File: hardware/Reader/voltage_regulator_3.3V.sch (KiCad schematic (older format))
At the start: 8 parts

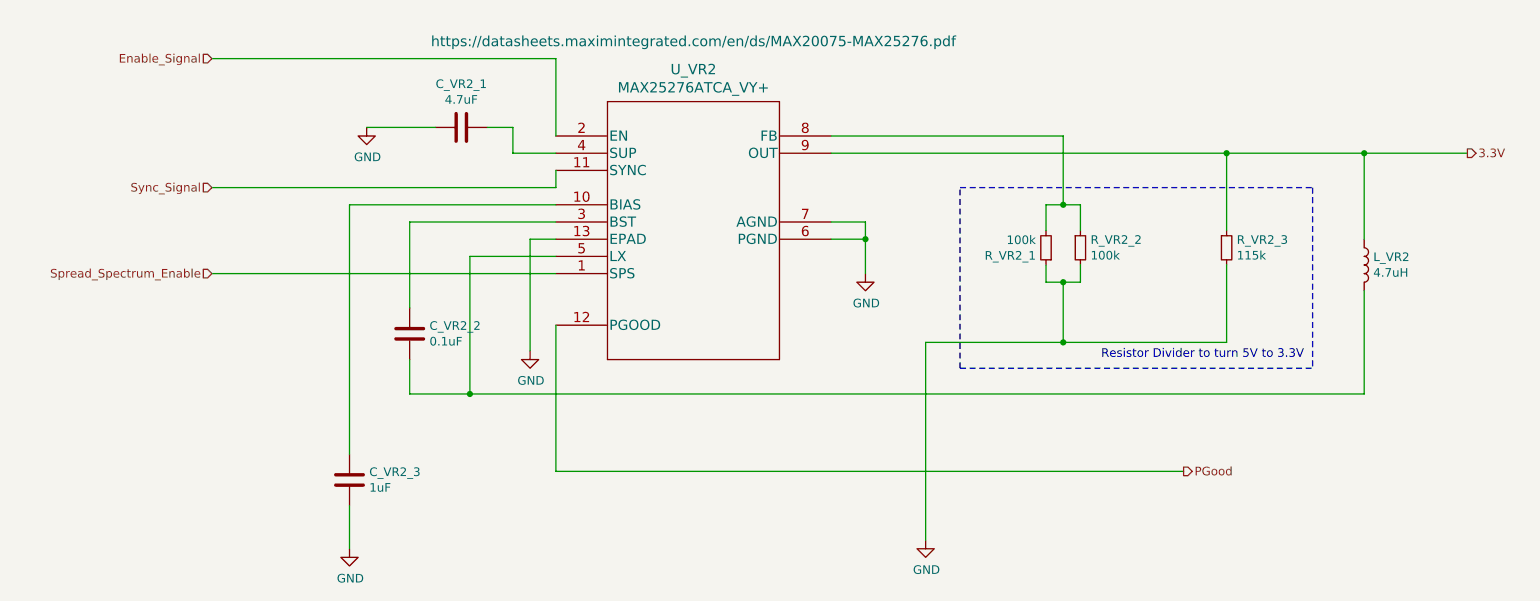
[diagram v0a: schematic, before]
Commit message: Fixed numerous bugs in design for Reader Schematic and PCB
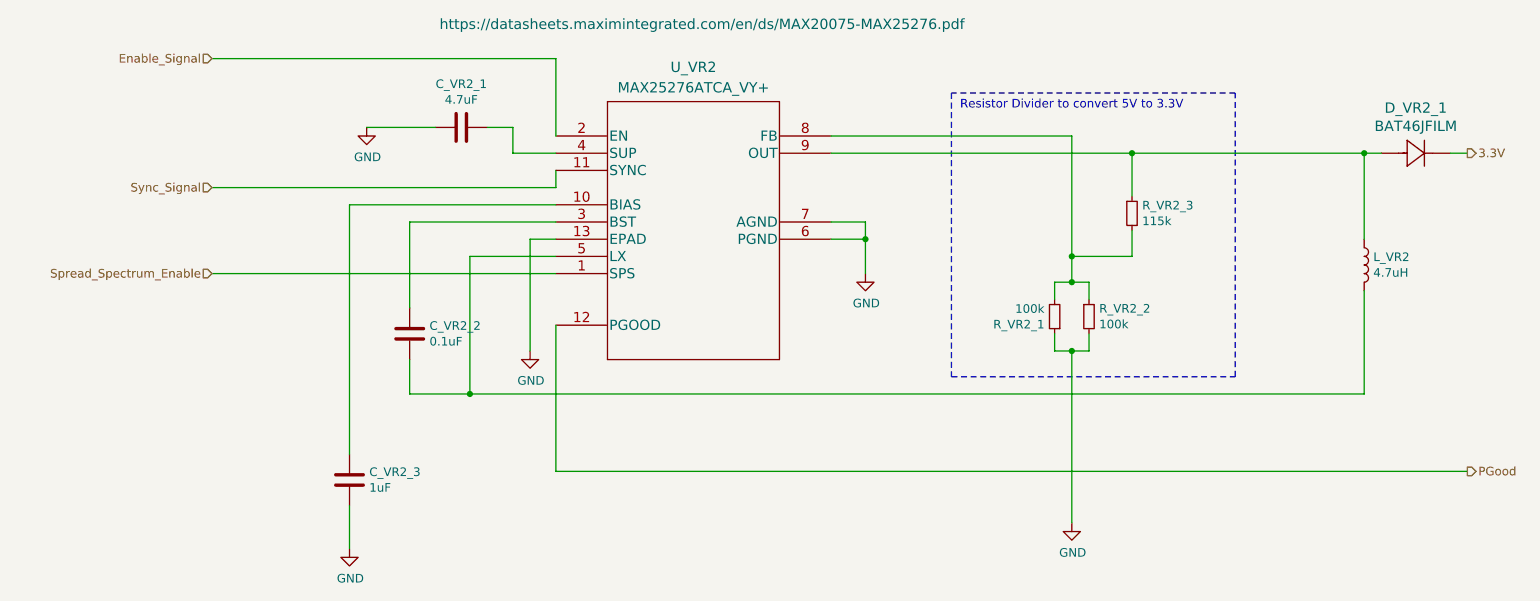
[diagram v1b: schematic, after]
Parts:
- added D_VR2_1: BAT46JFILM, footprints:BAT46JFILM, symbol BAT46:BAT46
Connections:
- net 3.3V: now also D_VR2_1.1; no longer L_VR2.1, R_VR2_3.1, U_VR2.9 (OUT)
- net GND: no longer R_VR2_3.2
- net at R_VR2_1.2, R_VR2_2.1, U_VR2.8 (FB): now also R_VR2_3.2
- new net: D_VR2_1.2, L_VR2.1, R_VR2_3.1, U_VR2.9 (OUT)
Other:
- note added: "Resistor Divider to convert 5V to 3.3V"
- note removed: "Resistor Divider to turn 5V to 3.3V"
- moved on the sheet: R_VR2_1, R_VR2_2, R_VR2_3

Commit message: Updated reader schematic to v0.0.5 by adding ESP32, removing unused transceivers, fixed design flaws, increased header pins and fixed footprints. Working on reader PCB design
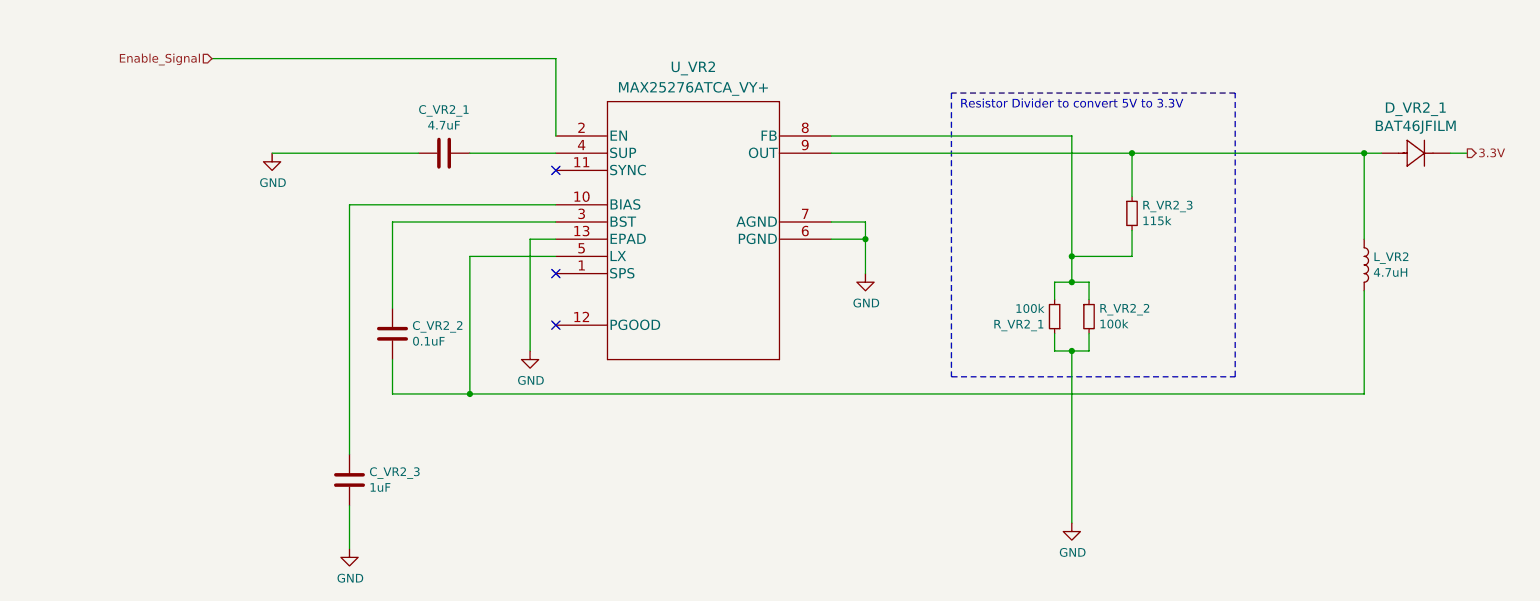
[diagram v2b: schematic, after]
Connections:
- net PGood: no longer names the net of U_VR2.12 (PGOOD)
- net Spread_Spectrum_Enable: no longer names the net of U_VR2.1 (SPS)
- net Sync_Signal: no longer names the net of U_VR2.11 (SYNC)
- no-connect marks 0 -> 3
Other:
- moved on the sheet: C_VR2_1, C_VR2_2
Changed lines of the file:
@@
 $Descr USLetter 11000 8500
 encoding utf-8
-Sheet 17 19
+Sheet 8 17
 Title "CANnect Reader | Voltage Regulator (3.3V)"
-Date "2020-11-19"
+Date "2020-11-27"
 Rev "0.0.05"
 Comp "CANtech"
@@
 Text HLabel 9750 2400 2    50   Output ~ 0
 3.3V
-Text HLabel 9750 4250 2    50   Output ~ 0
-PGood
 $Comp
 L power:GND #PWR?
@@
 Wire Wire Line
 	4450 1850 4450 2300
-Wire Wire Line
-	4450 2600 4450 2500
-Wire Wire Line
-	4450 3400 4450 4250
 $Comp
 L Device:L L_VR?
@@
 	9150 2900 9150 2400
 $Comp
-L Device:C C_VR2_BST?
-U 1 1 5FF31636
-P 3600 3450
-AR Path="/5F8ADA45/5F9EA8B0/5FF31636" Ref="C_VR2_BST?"  Part="1"
-AR Path="/5F8ADA45/5FF30350/5FF31636" Ref="C_VR2_2"  Part="1"
-F 0 "C_VR2_2" H 3715 3496 50  0000 L CNN
-F 1 "0.1uF" H 3715 3405 50  0000 L CNN
-F 2 "footprints:CAPC1608X90" H 3638 3300 50  0001 C CNN
-F 3 "https://www.yageo.com/upload/media/product/productsearch/datasheet/mlcc/UPY-GPHC_X7R_6.3V-to-50V_18.pdf" H 3600 3450 50  0001 C CNN
-F 4 "CC0603JRX7R8BB104" H 3600 3450 50  0001 C CNN "Part Name"
-F 5 "Yageo" H 3600 3450 50  0001 C CNN "Manufacturer"
-F 6 "DigiKey Canada" H 3600 3450 50  0001 C CNN "Vendor"
-F 7 "311-1777-1-ND" H 3600 3450 50  0001 C CNN "digikeypn"
-	1    3600 3450
-	1    0    0    -1
-$EndComp
-$Comp
 L power:GND #PWR?
 U 1 1 5FF3163C
@@
 Wire Wire Line
 	4300 2900 4450 2900
-Wire Wire Line
-	4450 2800 3600 2800
-Wire Wire Line
-	3600 2800 3600 3300
-Wire Wire Line
-	3600 3600 3600 3800
-Wire Wire Line
-	3600 3800 3950 3800
 Wire Wire Line
 	9150 3800 9150 3200
@@
 	7350 3550 7350 3450
 Connection ~ 7450 3550
-$Comp
-L MAX25276ATCAVY:MAX25276ATCA_VY+ U_VR?
-U 1 1 5FF315FD
-P 4450 2300
-AR Path="/5F8ADA45/5F9EA8B0/5FF315FD" Ref="U_VR?"  Part="1"
-AR Path="/5F8ADA45/5FF30350/5FF315FD" Ref="U_VR2"  Part="1"
-F 0 "U_VR2" H 5250 2700 60  0000 C CNN
-F 1 "MAX25276ATCA_VY+" H 5250 2581 60  0000 C CNN
-F 2 "footprints:MAX25276ATCA&slash_VY&plus_" H 5250 2540 60  0001 C CNN
-F 3 "https://datasheets.maximintegrated.com/en/ds/MAX20075-MAX25276.pdf" H 5300 2950 60  0000 C CNN
-F 4 "MAX25276ATCA/VY+" H 4450 2300 50  0001 C CNN "Part Name"
-F 5 "Maxim Integrated" H 4450 2300 50  0001 C CNN "Manufacturer"
-F 6 "DigiKey Canada" H 4450 2300 50  0001 C CNN "Vendor"
-F 7 "175-MAX25276ATCA/VY+-ND" H 4450 2300 50  0001 C CNN "digikeypn"
-	1    4450 2300
-	1    0    0    -1
-$EndComp
-Wire Wire Line
-	4450 2400 4200 2400
-Wire Wire Line
-	4200 2400 4200 2250
-Wire Wire Line
-	4450 4250 9750 4250
 Wire Wire Line
 	6050 2300 7450 2300
@@
 	1    0    0    -1
 $EndComp
-Wire Wire Line
-	4200 2250 4050 2250
 $Comp
 L Device:C C_VR2_in?
 U 1 1 5FF3161F
-P 3900 2250
+P 3800 2400
 AR Path="/5F8ADA45/5F9EA8B0/5FF3161F" Ref="C_VR2_in?"  Part="1"
 AR Path="/5F8ADA45/5FF30350/5FF3161F" Ref="C_VR2_1"  Part="1"
-F 0 "C_VR2_1" V 3648 2250 50  0000 C CNN
-F 1 "4.7uF" V 3739 2250 50  0000 C CNN
-F 2 "footprints:C1206C475K3RACAUTO" H 3938 2100 50  0001 C CNN
-F 3 "https://api.kemet.com/component-edge/download/specsheet/C1206C475K3RACAUTO.pdf" H 3900 2250 50  0001 C CNN
-F 4 "C1206C475K3RACAUTO" H 3900 2250 50  0001 C CNN "Part Name"
-F 5 "Kermet" H 3900 2250 50  0001 C CNN "Manufacturer"
-F 6 "DigiKey Canada" H 3900 2250 50  0001 C CNN "Vendor"
-F 7 "399-7029-1-ND" H 3900 2250 50  0001 C CNN "digikeypn"
-	1    3900 2250
+F 0 "C_VR2_1" V 3548 2400 50  0000 C CNN
+F 1 "4.7uF" V 3639 2400 50  0000 C CNN
+F 2 "footprints:C1206C475K3RACAUTO" H 3838 2250 50  0001 C CNN
+F 3 "https://api.kemet.com/component-edge/download/specsheet/C1206C475K3RACAUTO.pdf" H 3800 2400 50  0001 C CNN
+F 4 "C1206C475K3RACAUTO" H 3800 2400 50  0001 C CNN "Part Name"
+F 5 "Kermet" H 3800 2400 50  0001 C CNN "Manufacturer"
+F 6 "DigiKey Canada" H 3800 2400 50  0001 C CNN "Vendor"
+F 7 "399-7029-1-ND" H 3800 2400 50  0001 C CNN "digikeypn"
+	1    3800 2400
 	0    1    1    0
 $EndComp
-Wire Wire Line
-	3350 2250 3750 2250
 $Comp
 L power:GND #PWR0108
 U 1 1 5F99A55F
-P 3350 2250
-F 0 "#PWR0108" H 3350 2000 50  0001 C CNN
-F 1 "GND" H 3355 2077 50  0000 C CNN
-F 2 "" H 3350 2250 50  0001 C CNN
-F 3 "" H 3350 2250 50  0001 C CNN
-	1    3350 2250
-	1    0    0    -1
-$EndComp
-Wire Wire Line
-	2450 3100 4450 3100
-Text HLabel 2450 3100 0    50   Input ~ 0
-Spread_Spectrum_Enable
-Wire Wire Line
-	2450 2600 4450 2600
-Text HLabel 2450 2600 0    50   Input ~ 0
-Sync_Signal
+P 2800 2400
+F 0 "#PWR0108" H 2800 2150 50  0001 C CNN
+F 1 "GND" H 2805 2227 50  0000 C CNN
+F 2 "" H 2800 2400 50  0001 C CNN
+F 3 "" H 2800 2400 50  0001 C CNN
+	1    2800 2400
+	1    0    0    -1
+$EndComp
 Wire Wire Line
 	2450 1850 4450 1850
@@
 Wire Wire Line
 	9650 2400 9750 2400
+NoConn ~ 4450 3100
+NoConn ~ 4450 3400
+Wire Wire Line
+	3500 3600 3500 3800
+Wire Wire Line
+	3500 2800 3500 3300
+$Comp
+L Device:C C_VR2_BST?
+U 1 1 5FF31636
+P 3500 3450
+AR Path="/5F8ADA45/5F9EA8B0/5FF31636" Ref="C_VR2_BST?"  Part="1"
+AR Path="/5F8ADA45/5FF30350/5FF31636" Ref="C_VR2_2"  Part="1"
+F 0 "C_VR2_2" H 3615 3496 50  0000 L CNN
+F 1 "0.1uF" H 3615 3405 50  0000 L CNN
+F 2 "footprints:CAPC1608X90" H 3538 3300 50  0001 C CNN
+F 3 "https://www.yageo.com/upload/media/product/productsearch/datasheet/mlcc/UPY-GPHC_X7R_6.3V-to-50V_18.pdf" H 3500 3450 50  0001 C CNN
+F 4 "CC0603JRX7R8BB104" H 3500 3450 50  0001 C CNN "Part Name"
+F 5 "Yageo" H 3500 3450 50  0001 C CNN "Manufacturer"
+F 6 "DigiKey Canada" H 3500 3450 50  0001 C CNN "Vendor"
+F 7 "311-1777-1-ND" H 3500 3450 50  0001 C CNN "digikeypn"
+	1    3500 3450
+	1    0    0    -1
+$EndComp
+Wire Wire Line
+	3500 2800 4450 2800
+Wire Wire Line
+	3500 3800 3950 3800
+$Comp
+L MAX25276ATCAVY:MAX25276ATCA_VY+ U_VR?
+U 1 1 5FF315FD
+P 4450 2300
+AR Path="/5F8ADA45/5F9EA8B0/5FF315FD" Ref="U_VR?"  Part="1"
+AR Path="/5F8ADA45/5FF30350/5FF315FD" Ref="U_VR2"  Part="1"
+F 0 "U_VR2" H 5250 2700 60  0000 C CNN
+F 1 "MAX25276ATCA_VY+" H 5250 2581 60  0000 C CNN
+F 2 "footprints:MAX25276ATCA&slash_VY&plus_" H 5250 2540 60  0001 C CNN
+F 3 "https://datasheets.maximintegrated.com/en/ds/MAX20075-MAX25276.pdf" H 5300 2950 60  0001 C CNN
+F 4 "MAX25276ATCA/VY+" H 4450 2300 50  0001 C CNN "Part Name"
+F 5 "Maxim Integrated" H 4450 2300 50  0001 C CNN "Manufacturer"
+F 6 "DigiKey Canada" H 4450 2300 50  0001 C CNN "Vendor"
+F 7 "175-MAX25276ATCA/VY+-ND" H 4450 2300 50  0001 C CNN "digikeypn"
+	1    4450 2300
+	1    0    0    -1
+$EndComp
+NoConn ~ 4450 2500
+Wire Wire Line
+	3950 2400 4450 2400
+Wire Wire Line
+	3650 2400 2800 2400
 $EndSCHEMATC

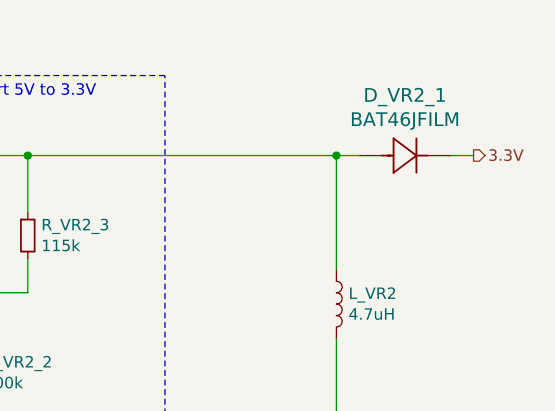
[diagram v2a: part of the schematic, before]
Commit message: Updated schematic and gerber to v0.0.05. Added ESP32. Removed MS CAN and SW CAN Transceivers. Added silkscreen text to header pins. Improved readability
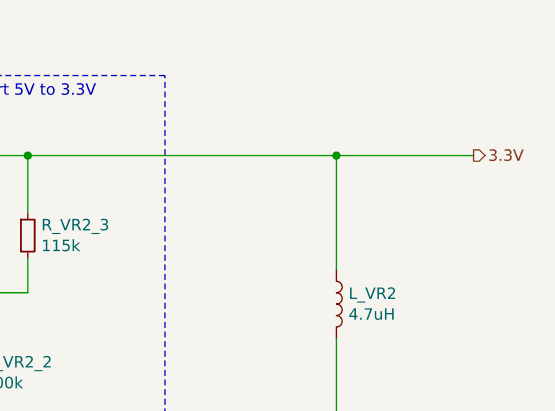
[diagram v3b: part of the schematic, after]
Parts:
- removed D_VR2_1: BAT46JFILM, footprints:BAT46JFILM, symbol BAT46:BAT46
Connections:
- net 3.3V: now also L_VR2.1, R_VR2_3.1, U_VR2.9 (OUT)
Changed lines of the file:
@@
 $Descr USLetter 11000 8500
 encoding utf-8
-Sheet 8 17
+Sheet 6 17
 Title "CANnect Reader | Voltage Regulator (3.3V)"
-Date "2020-11-27"
+Date "2020-11-29"
 Rev "0.0.05"
 Comp "CANtech"
@@
 Text HLabel 2450 1850 0    50   Input ~ 0
 Enable_Signal
-$Comp
-L BAT46:BAT46 D_VR2_1
-U 1 1 5FB95099
-P 9250 2400
-F 0 "D_VR2_1" H 9450 2663 60  0000 C CNN
-F 1 "BAT46JFILM" H 9450 2557 60  0000 C CNN
-F 2 "footprints:BAT46JFILM" H 9450 2040 60  0001 C CNN
-F 3 "https://www.st.com/content/ccc/resource/technical/document/datasheet/c6/32/d4/4a/28/d3/4b/11/CD00004930.pdf/files/CD00004930.pdf/jcr:content/translations/en.CD00004930.pdf" H 9450 2557 60  0001 C CNN
-F 4 "STMicroelectronics" H 9250 2400 50  0001 C CNN "Manufacturer"
-F 5 "BAT46JFILM" H 9250 2400 50  0001 C CNN "Part Name"
-F 6 "DigiKey Canada" H 9250 2400 50  0001 C CNN "Vendor"
-F 7 "497-6653-1-ND" H 9250 2400 50  0001 C CNN "digikeypn"
-	1    9250 2400
-	1    0    0    -1
-$EndComp
-Wire Wire Line
-	9150 2400 9250 2400
 Connection ~ 9150 2400
-Wire Wire Line
-	9650 2400 9750 2400
 NoConn ~ 4450 3100
 NoConn ~ 4450 3400
@@
 Wire Wire Line
 	3650 2400 2800 2400
+Wire Wire Line
+	9150 2400 9750 2400
 $EndSCHEMATC
